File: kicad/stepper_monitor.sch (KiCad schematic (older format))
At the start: 1 part, among them U1 ESP32-WROOM-32

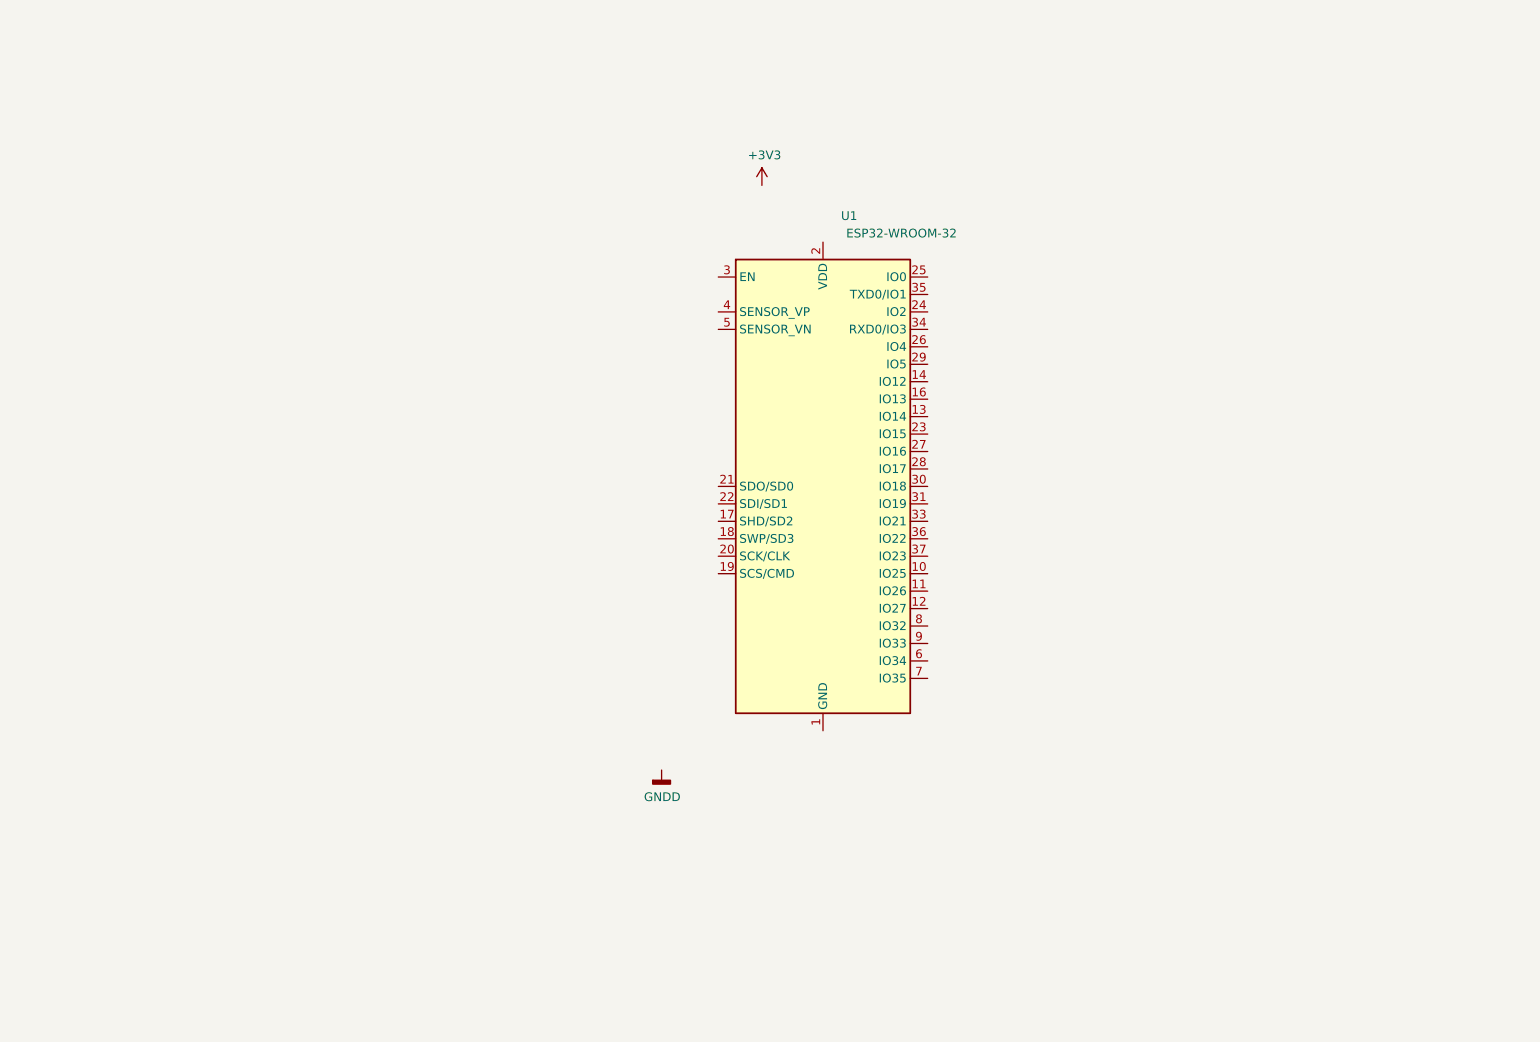
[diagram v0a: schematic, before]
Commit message: Updated to Kicad 6
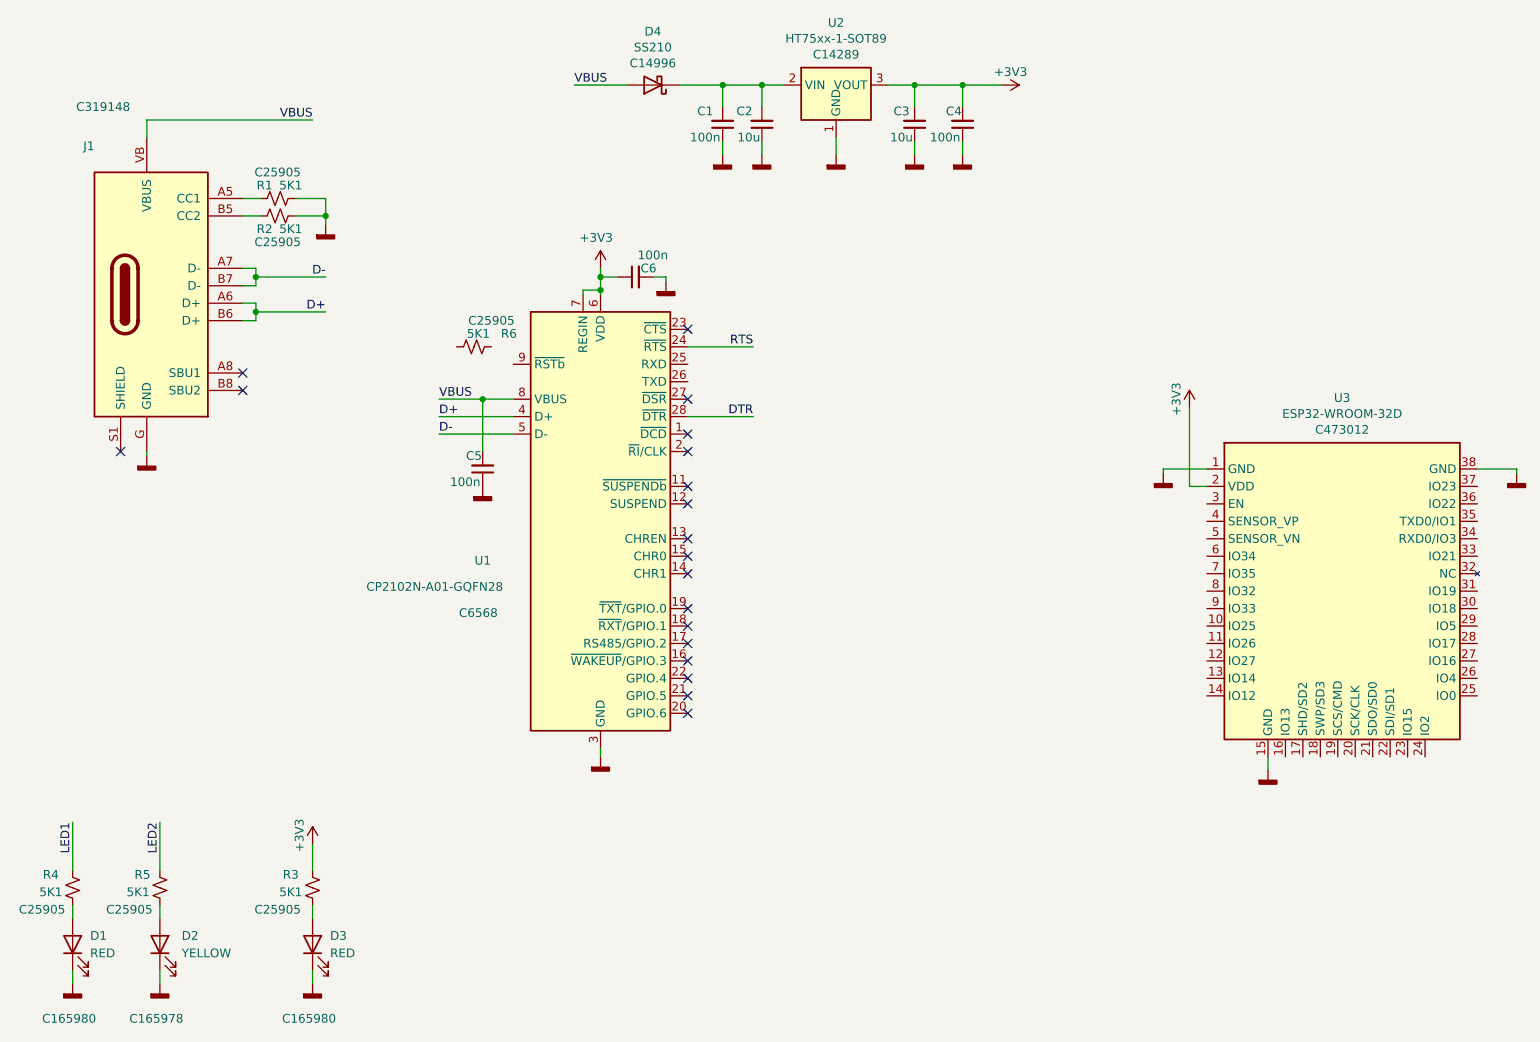
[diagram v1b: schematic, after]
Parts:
- removed U1: ESP32-WROOM-32, RF_Module:ESP32-WROOM-32, symbol RF_Module:ESP32-WROOM-32
- added C1, C4, C5, C6: 100n, Capacitor_SMD:C_0402_1005Metric, symbol Device:C_Small
- added C2, C3: 10u, Capacitor_SMD:C_0402_1005Metric, symbol Device:C_Small
- added D1, D3: RED, symbol Device:LED
- added D2: YELLOW, symbol Device:LED
- added D4: SS210, symbol Device:D_Schottky
- added J1: USB_C_Receptacle_USB2.0, stepper_monitor:USB_C_Receptacle_XKB_U262-16XN-4BVC11, symbol stepper_monitor:USB_C_Receptacle_USB2.0
- added R1, R2, R3, R4, R5, R6: 5K1, Resistor_SMD:R_0402_1005Metric, symbol Device:R_Small_US
- added U1: CP2102N-A01-GQFN28, Package_DFN_QFN:QFN-28-1EP_5x5mm_P0.5mm_EP3.35x3.35mm, symbol Interface_USB:CP2102N-A01-GQFN28
- added U2: HT75xx-1-SOT89, Package_TO_SOT_SMD:SOT-89-3, symbol stepper_monitor:HT75xx-1-SOT89
- added U3: ESP32-WROOM-32D, RF_Module:ESP32-WROOM-32, symbol stepper_monitor:ESP32-WROOM-32D
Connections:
- net +3V3: now also C3.2, C4.2, C6.1, R3.2, U1.6 (VDD), U1.7 (REGIN), U2.3 (VOUT), U3.2 (VDD)
- net GNDD: now also C1.1, C2.1, C3.1, C4.1, C5.1, C6.2, D1.1 (K), D2.1 (K), D3.1 (K), J1.G (GND), R1.1, R2.1, U1.29 (GND), U1.3 (GND), U2.1 (GND), U3.1 (GND), U3.15 (GND), U3.38 (GND), U3.39 (GND)
- new net: J1.B5 (CC2), R2.2
- new net: J1.A5 (CC1), R1.2
- new net: C1.2, C2.2, D4.1 (K), U2.2 (VIN)
- new net: D3.2 (A), R3.1
- new net: D1.2 (A), R4.1
- new net: D2.2 (A), R5.1
- new net D+: J1.A6 (D+), J1.B6 (D+), U1.4 (D+)
- new net D-: J1.A7 (D-), J1.B7 (D-), U1.5 (D-)
- new net DTR: U1.28 (~DTR)
- new net LED1: R4.2
- new net LED2: R5.2
- new net RTS: U1.24 (~RTS)
- new net VBUS: C5.2, D4.2 (A), J1.VB (VBUS), U1.8 (VBUS)
- no-connect marks 0 -> 19
